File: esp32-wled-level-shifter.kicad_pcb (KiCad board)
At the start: 2 copper layers, 28.4 x 59.9 mm, 5 parts, among them J1 Conn_01x04_Female, J2 Conn_01x15_Female, J3 Conn_01x15_Female, U1 CD40106

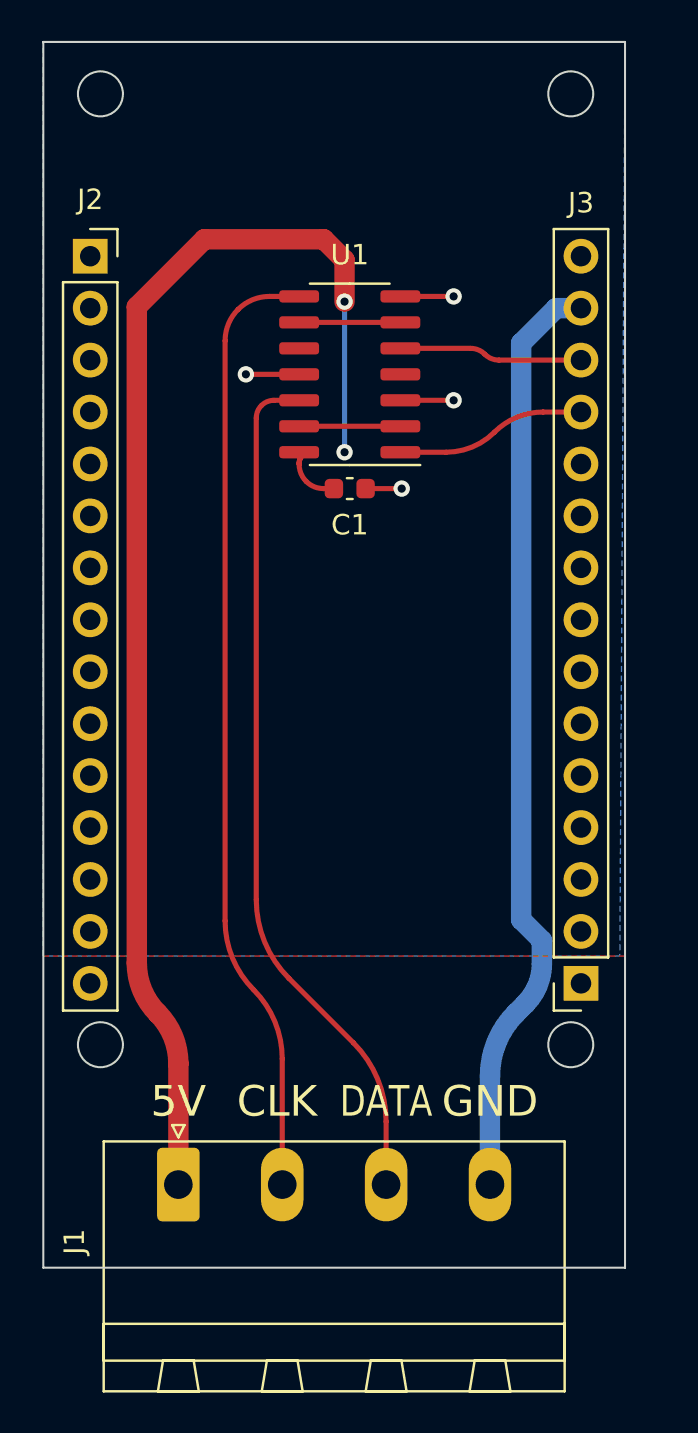
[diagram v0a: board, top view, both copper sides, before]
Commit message: Dimension and size tweaks
- Correctly space connectors
- Increase size of mounting holes, allow M3
- Chamfer board edges
- More silkscreen markings
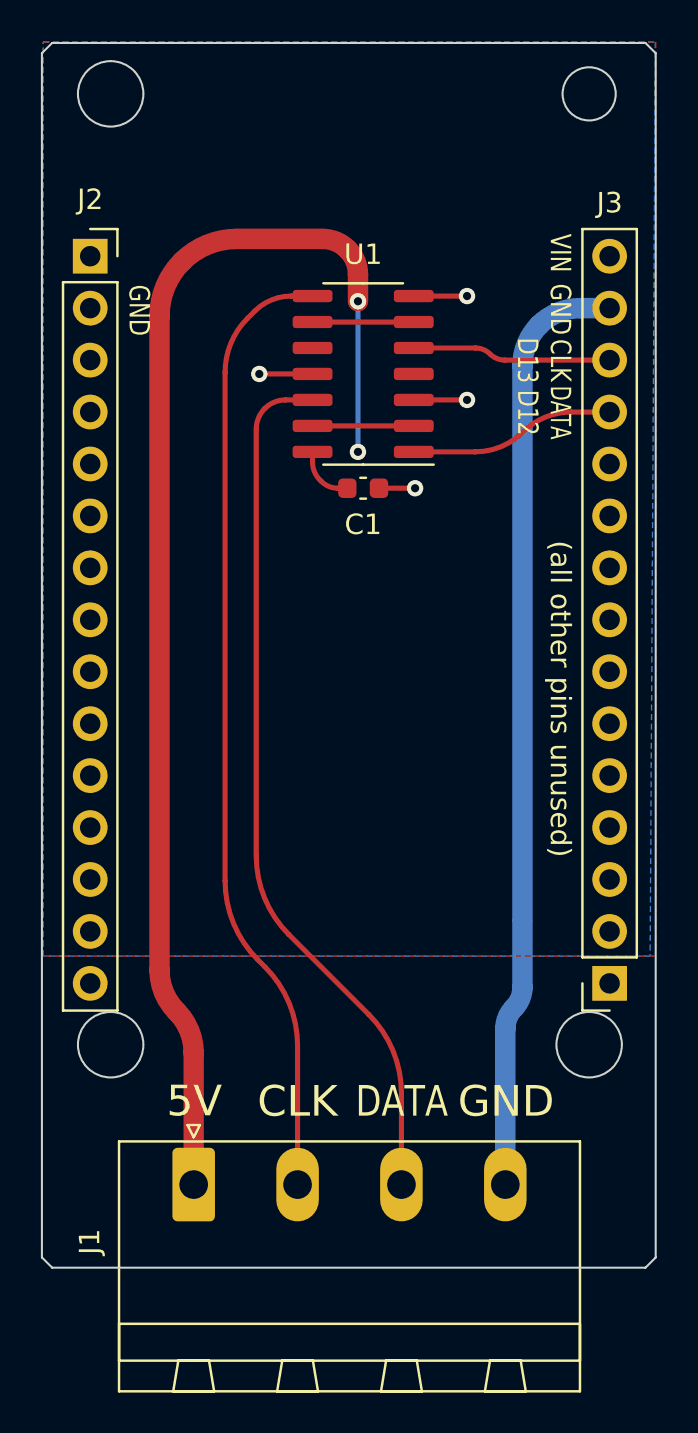
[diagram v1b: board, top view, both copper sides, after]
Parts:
- moved J3 1.40 mm to (159.0, 104.7)
- moved J1 0.75 mm to (138.7, 114.6)
- moved C1 0.66 mm to (147.0, 80.5)
- moved U1 0.66 mm to (147.0, 74.9)
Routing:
- net +5V: track 68.9 -> 67.3 mm
- net /CLK_3V3: track 8.98 -> 9.73 mm
- net /DATA_3V3: track 9.32 -> 10.1 mm
- net /DATA_5V: track 42.2 -> 42.9 mm
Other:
- board size 28.4 x 59.9 mm -> 30 x 59.9 mm
- board text added: "(all other pins unused)"
- board text added: "CLK D13"
- board text added: "D12"
- board text added: "ESP32 WLED APA102 LEVEL SHIFTER REV.1 MICHD - JUNE 2022"
- board text added: "VIN"
- board text removed: "ESP32 WLED APA102 LEVEL SHIFTER REV.0 MICHD - MAY 2022"

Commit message: Rev2 board with experimenting playground
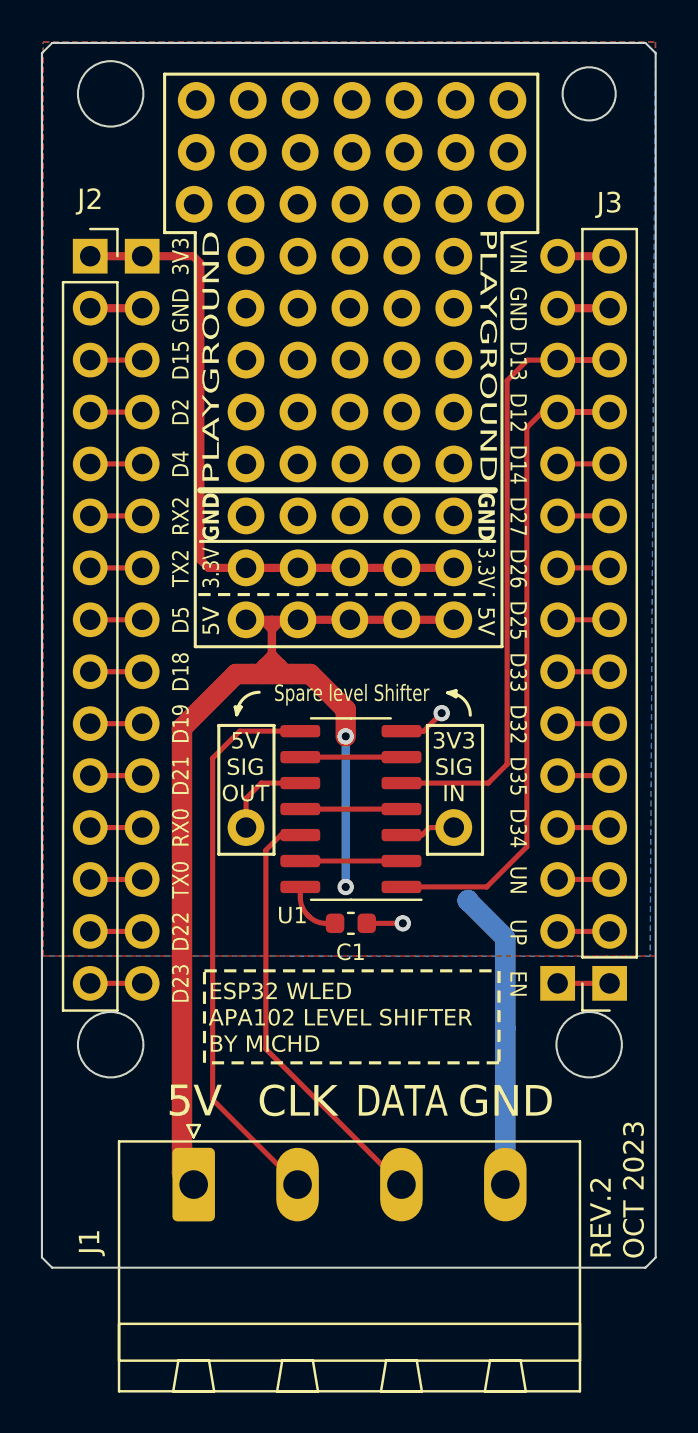
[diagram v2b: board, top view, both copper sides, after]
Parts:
- added ?: , , F.Cu at (141.2, 79.3)
- added ?: , , F.Cu at (143.8, 76.8)
- added ?: , , F.Cu at (146.3, 74.2)
- added ?: , , F.Cu at (138.7, 66.6)
- added ?: , , F.Cu at (148.9, 84.4)
- added ?: , , F.Cu at (143.8, 74.2)
- added ?: , , F.Cu at (141.2, 71.7)
- added ?: , , F.Cu at (143.9, 64.1)
- added ?: , , F.Cu at (149.0, 64.1)
- added ?: , , F.Cu at (146.3, 81.9)
- added ?: , , F.Cu at (148.9, 86.9)
- added ?: , , F.Cu at (151.4, 79.3)
- added ?: , , F.Cu at (143.8, 81.9)
- added ?: , , F.Cu at (148.9, 71.7)
- added ?: , , F.Cu at (143.8, 79.3)
- added ?: , , F.Cu at (141.2, 69.2)
- added ?: , , F.Cu at (143.8, 66.6)
- added ?: , , F.Cu at (141.2, 74.2)
- added ?: , , F.Cu at (151.4, 81.9)
- added ?: , , F.Cu at (148.9, 81.9)
- added ?: , , F.Cu at (149.0, 61.5)
- added ?: , , F.Cu at (154.0, 61.5)
- added ?: , , F.Cu at (141.3, 61.5)
- added ?: , , F.Cu at (141.2, 84.4)
- added ?: , , F.Cu at (151.4, 74.2)
- added ?: , , F.Cu at (146.3, 86.9)
- added ?: , , F.Cu at (141.3, 64.1)
- added ?: , , F.Cu at (146.3, 66.6)
- added ?: , , F.Cu at (151.4, 84.4)
- added ?: , , F.Cu at (141.2, 76.8)
- added ?: , , F.Cu at (151.5, 64.1)
- added ?: , , F.Cu at (138.8, 64.1)
- added ?: , , F.Cu at (141.2, 86.9)
- added ?: , , F.Cu at (141.2, 81.9)
- added ?: , , F.Cu at (148.9, 66.6)
- added ?: , , F.Cu at (146.3, 76.8)
- added ?: , , F.Cu at (146.4, 61.5)
- added ?: , , F.Cu at (146.3, 69.2)
- added ?: , , F.Cu at (143.8, 69.2)
- added ?: , , F.Cu at (154.0, 64.1)
- added ?: , , F.Cu at (141.2, 66.6)
- added ?: , , F.Cu at (146.3, 71.7)
- added ?: , , F.Cu at (143.8, 84.4)
- added ?: , , F.Cu at (143.8, 86.9)
- added ?: , , F.Cu at (151.4, 76.8)
- added ?: , , F.Cu at (148.9, 76.8)
- added ?: , , F.Cu at (151.4, 66.6)
- added ?: , , F.Cu at (151.4, 87.0)
- added ?: , , F.Cu at (148.9, 69.2)
- added ?: , , F.Cu at (151.5, 61.5)
- added ?: , , F.Cu at (146.4, 64.1)
- added ?: , , F.Cu at (148.9, 74.2)
- added ?: , , F.Cu at (151.4, 69.5)
- added ?: , , F.Cu at (146.3, 79.3)
- added ?: , , F.Cu at (143.9, 61.5)
- added ?: , , F.Cu at (146.3, 84.4)
- added ?: , , F.Cu at (138.8, 61.5)
- added ?: , , F.Cu at (143.8, 71.7)
- added ?: , , F.Cu at (153.9, 66.6)
- added ?: , , F.Cu at (148.9, 79.3)
- added ?: , , F.Cu at (151.4, 71.7)
- added J4: Conn_01x15_Female, Connector_PinSocket_2.54mm:PinSocket_1x15_P2.54mm_Vertical, F.Cu at (136.2, 69.2)
- added J5: Conn_01x15_Female, Connector_PinSocket_2.54mm:PinSocket_1x15_P2.54mm_Vertical, F.Cu at (156.5, 104.7)
- added TP1: TestPoint, TestPoint:TestPoint_THTPad_D2.0mm_Drill1.0mm, F.Cu at (151.4, 97.1)
- added TP2: TestPoint, TestPoint:TestPoint_THTPad_D2.0mm_Drill1.0mm, F.Cu at (141.2, 97.1)
- moved C1 21.3 mm to (146.4, 101.8)
- moved U1 21.3 mm to (146.4, 96.2)
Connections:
- J2 pad 1: unconnected-(J2-Pad1) -> +3.3V
- J2 pad 10: unconnected-(J2-Pad10) -> Net-(J2-Pin_10)
- J2 pad 11: unconnected-(J2-Pad11) -> Net-(J2-Pin_11)
- J2 pad 12: unconnected-(J2-Pad12) -> Net-(J2-Pin_12)
- J2 pad 13: unconnected-(J2-Pad13) -> Net-(J2-Pin_13)
- J2 pad 14: unconnected-(J2-Pad14) -> Net-(J2-Pin_14)
- J2 pad 15: unconnected-(J2-Pad15) -> Net-(J2-Pin_15)
- J2 pad 3: unconnected-(J2-Pad3) -> Net-(J2-Pin_3)
- J2 pad 4: unconnected-(J2-Pad4) -> Net-(J2-Pin_4)
- J2 pad 5: unconnected-(J2-Pad5) -> Net-(J2-Pin_5)
- J2 pad 6: unconnected-(J2-Pad6) -> Net-(J2-Pin_6)
- J2 pad 7: unconnected-(J2-Pad7) -> Net-(J2-Pin_7)
- J2 pad 8: unconnected-(J2-Pad8) -> Net-(J2-Pin_8)
- J2 pad 9: unconnected-(J2-Pad9) -> Net-(J2-Pin_9)
- J3 pad 1: unconnected-(J3-Pad1) -> Net-(J3-Pin_1)
- J3 pad 10: unconnected-(J3-Pad10) -> Net-(J3-Pin_10)
- J3 pad 11: unconnected-(J3-Pad11) -> Net-(J3-Pin_11)
- J3 pad 2: unconnected-(J3-Pad2) -> Net-(J3-Pin_2)
- J3 pad 3: unconnected-(J3-Pad3) -> Net-(J3-Pin_3)
- J3 pad 4: unconnected-(J3-Pad4) -> Net-(J3-Pin_4)
- J3 pad 5: unconnected-(J3-Pad5) -> Net-(J3-Pin_5)
- J3 pad 6: unconnected-(J3-Pad6) -> Net-(J3-Pin_6)
- J3 pad 7: unconnected-(J3-Pad7) -> Net-(J3-Pin_7)
- J3 pad 8: unconnected-(J3-Pad8) -> Net-(J3-Pin_8)
- J3 pad 9: unconnected-(J3-Pad9) -> Net-(J3-Pin_9)
- U1 pad 10: unconnected-(U1-Pad10) -> Net-(TP2-Pad1)
- U1 pad 11: GND -> Net-(U1-Pad11)
- U1 pad 3: GND -> Net-(TP1-Pad1)
- U1 pad 4: unconnected-(U1-Pad4) -> Net-(U1-Pad11)
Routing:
- net +3.3V: track 0.00 -> 32.6 mm
- net GND: track 55.6 -> 23.3 mm, vias 4 -> 2
- net /DATA_3V3: track 10.1 -> 34.3 mm
- net /CLK_3V3: track 9.73 -> 32.3 mm
- net /DATA_5V: track 42.9 -> 21.1 mm
- net /CLK_5V: track 47.1 -> 28.0 mm
- net Net-(U1-Pad11): track 0.00 -> 4.95 mm
- net Net-(TP2-Pad1): track 0.00 -> 4.39 mm
- net Net-(TP1-Pad1): track 0.00 -> 2.82 mm
- net Net-(J3-Pin_9): track 0.00 -> 2.54 mm
- net Net-(J3-Pin_8): track 0.00 -> 2.54 mm
- net Net-(J3-Pin_7): track 0.00 -> 2.54 mm
- net Net-(J3-Pin_6): track 0.00 -> 2.54 mm
- net Net-(J3-Pin_5): track 0.00 -> 2.54 mm
- net Net-(J3-Pin_4): track 0.00 -> 2.54 mm
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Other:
- board text added: "3.3V"
- board text added: "3V3"
- board text added: "3V3 SIG IN"
- board text added: "5V SIG OUT"
- board text added: "CD40106"
- board text added: "D13"
- board text added: "D14"
- board text added: "D15"
- board text added: "D18"
- board text added: "D19"
- board text added: "D2"
- board text added: "D21"
- board text added: "D22"
- board text added: "D23"
- board text added: "D25"
- board text added: "D26"
- board text added: "D27"
- board text added: "D32"
- board text added: "D33"
- board text added: "D34"
- board text added: "D35"
- board text added: "D4"
- board text added: "D5"
- board text added: "EN"
- board text added: "ESP32 WLED APA102 LEVEL SHIFTER BY MICHD"
- board text added: "PLAYGROUND"
- board text added: "REV.2 OCT 2023"
- board text added: "RX0"
- board text added: "RX2"
- board text added: "Spare level Shifter"
- board text added: "TP1"
- board text added: "TP2"
- board text added: "TX0"
- board text added: "TX2"
- board text added: "U1"
- board text added: "UN"
- board text added: "UP"
- board text removed: "(all other pins unused)"
- board text removed: "CLK D13"
- board text removed: "ESP32 WLED APA102 LEVEL SHIFTER REV.1 MICHD - JUNE 2022"
